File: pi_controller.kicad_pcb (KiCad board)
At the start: 4 copper layers, 99.7 x 91.3 mm, 153 parts, among them J1 PWM, J10 AN4, J11 AN6, J12 AN8, J13 AN10, J14 AN14, J15 AN15, J16 AN2, J17 CS2, J18 CS4, J19 CS6, J2 DC Supply, J20 CS8, J21 CS3, J22 CS5, J23 CS7, J24 AN1, J25 AN16, J26 LED6, J27 LED5, J28 LED7, J29 LED8, J3 AN12, J30 I2C, J31 UART, J32 LED3, J33 LED1, J34 LED2, J35 LED4, J36 ROW1, J37 ROW2, J38 ROW3, J39 ROW5, J4 AN7, J40 ROW4, J41 ROW6, J42 ROW7, J43 ROW8, J5 AN9, J6 AN11, J7 AN5, J8 AN3, J9 AN13, Q1 AOD4184A, U1 AP62300TWU, U2 CD74HC4067SM96, U3 LM4040DBZ-3, U4 RaspberryPi_Pico, U5 74HC138, U6 TM1639 (TA2009B), U7 74HC138

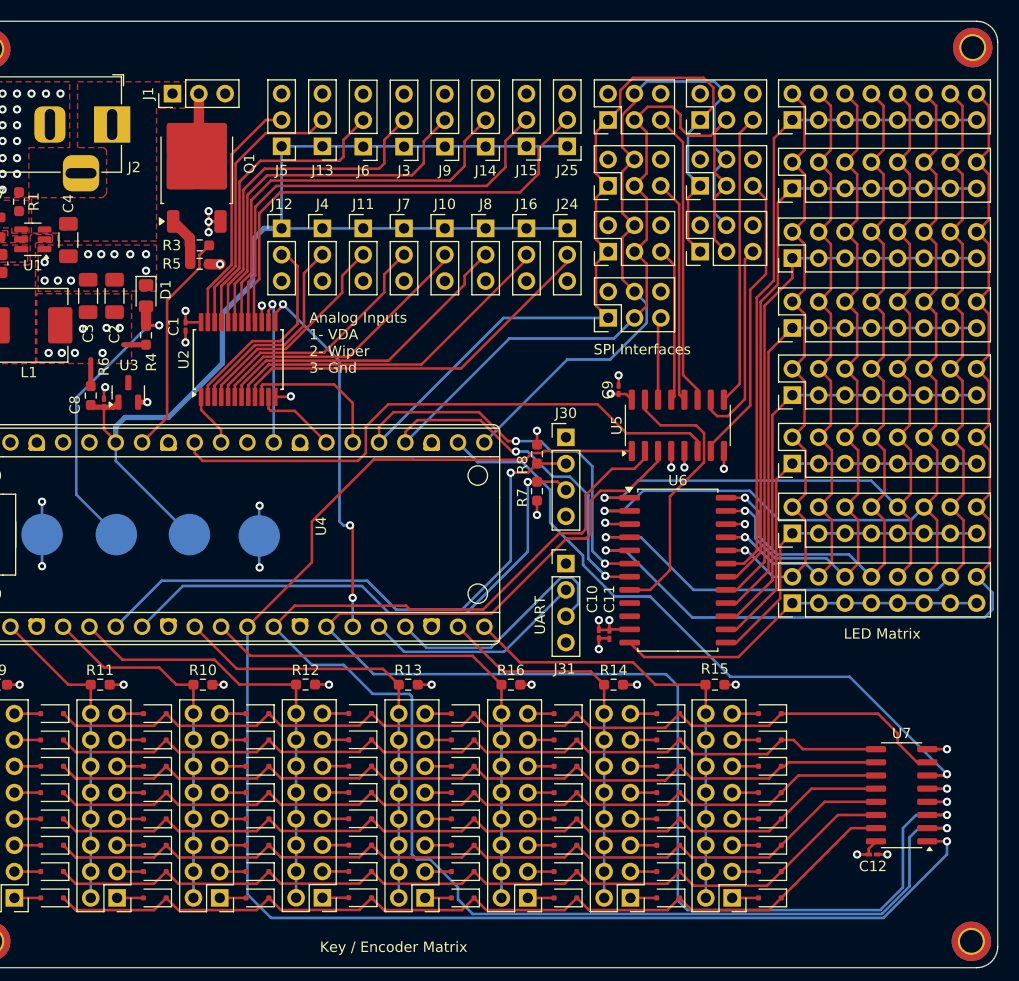
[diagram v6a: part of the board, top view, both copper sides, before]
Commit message: Adjusting component placement to have more room
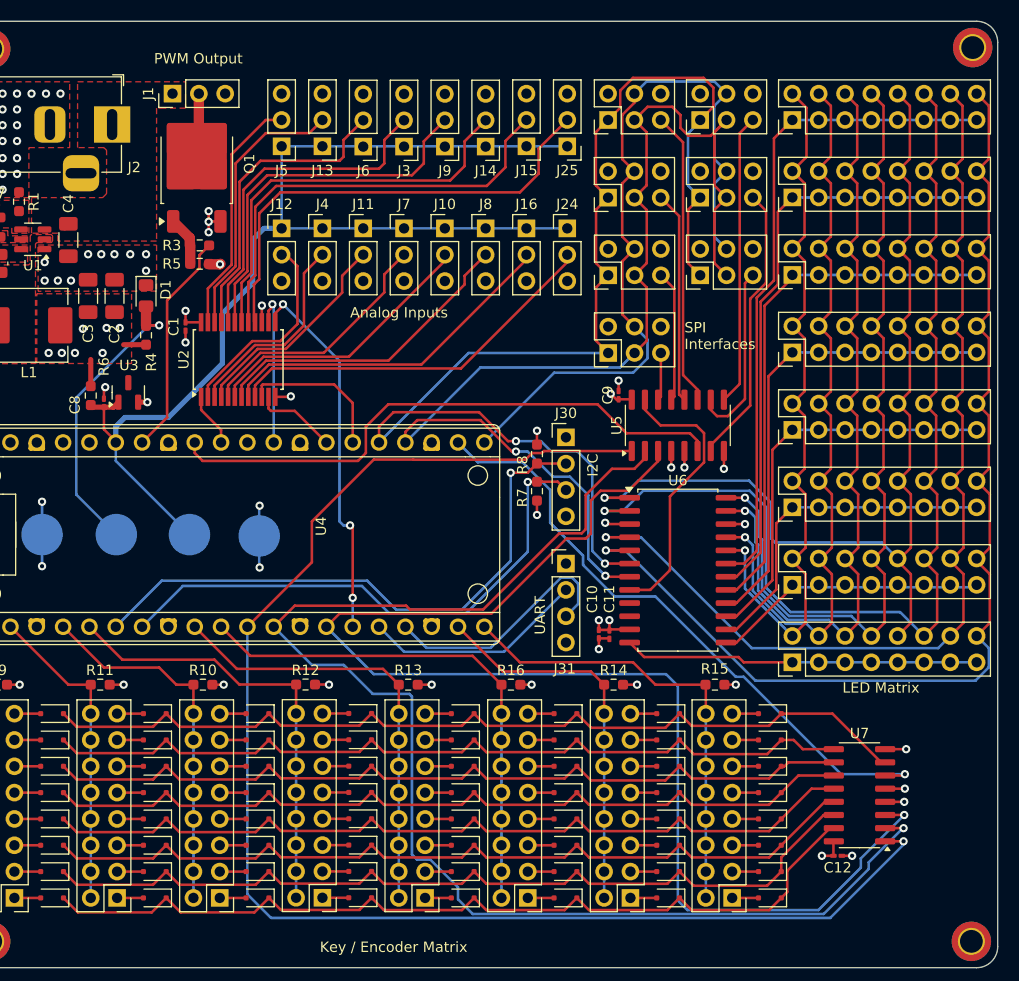
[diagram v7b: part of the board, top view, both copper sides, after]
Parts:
- moved J33 5.71 mm to (169.0, 118.0)
- moved J34 4.97 mm to (169.0, 110.5)
- moved J32 4.22 mm to (169.0, 103.0)
- moved U7 4.06 mm to (175.5, 130.8)
- moved C12 3.41 mm to (173.4, 136.7)
- moved J17 3.38 mm to (151.3, 88.1)
- moved J35 3.35 mm to (169.0, 95.6)
- moved J27 2.35 mm to (169.0, 88.1)
- moved J19 2.29 mm to (160.1, 80.6)
- moved J21 2.28 mm to (151.3, 80.6)
- moved J26 1.61 mm to (169.0, 80.6)
- moved J18 1.14 mm to (151.3, 73.2)
- moved J20 1.14 mm to (160.1, 73.2)
- moved J28 0.87 mm to (169.0, 73.1)
- moved C9 0.51 mm to (152.3, 92.2)
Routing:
- net /GRID3: track 89.4 -> 103.7 mm
- net /GRID5: track 72.1 -> 83.0 mm
- net /GRID6: track 68.8 -> 79.7 mm
- net /GRID7: track 64.1 -> 74.7 mm
- net /GRID8: track 61.0 -> 71.4 mm
- net /GRID4: track 86.1 -> 95.8 mm
- net /GRID2: track 91.9 -> 99.9 mm
- net /GRID1: track 100.1 -> 108.0 mm
- net /COL_MUX_C: track 133.8 -> 126.8 mm
- net /COL_MUX_B: track 139.6 -> 133.2 mm
- net /SEG2: track 31.6 -> 26.4 mm
- net /COL3: track 86.9 -> 82.2 mm
- net /COL_MUX_A: track 146.3 -> 141.6 mm
- net /COL8: track 92.8 -> 88.3 mm
- net /MISO: track 70.5 -> 74.9 mm
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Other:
- board text added: "Analog Inputs"
- board text added: "I2C"
- board text added: "PWM Output"
- board text removed: "Analog Inputs 1- VDA 2- Wiper 3- Gnd"
